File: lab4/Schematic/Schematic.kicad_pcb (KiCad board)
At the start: 2 copper layers, 121.5 x 269.9 mm, 408 parts, among them IC1 TPS564252DRLR, IC2 TPS564252DRLR, IC3 TPS564252DRLR, IC4 TPS564252DRLR, IC5 TPS564252DRLR, IC6 TPS564252DRLR, J1 XT60-M, J10 CANA_Z1, J11 CANA_Z1, J12 CANA_Z1, J13 CANA_Z1, J14 CANA_Z1, J15 CANA_Z1, J16 Conn_01x03_Pin, J17 Conn_01x03_Pin, J18 Barrel_Jack, J2 Z2_SWD, J3 Z2_SWD, J4 Z3_USART, J5 Raspberry_Pi_4, J6 Z3_USART, J7 MOTOR_RIGHT, J8 MOTOR_LEFT, J9 SERVO, Q2 IRF4905, U1 MCP2515-xST, U10 SN65HVD230, U11 MCP2515-xST, U12 SN65HVD230, U13 MCP2515-xST, U14 SN65HVD230, U15 MCP2515-xST, U16 SN65HVD230, U17 MCP2515-xST, U18 SN65HVD230, U2 ACS712xLCTR-05B, U20 L298N, U3 STM32F401RETx, U4 ACS712xLCTR-05B, U5 INA181, U7 STM32F401RETx, U8 SN65HVD230, U9 MCP2515-xST, Y1 CX3225SB16000H0FLJCC, Y2 CX3225SB16000H0FLJCC, Y3 CX3225SB16000H0FLJCC, Y4 CX3225SB16000H0FLJCC, Y5 CX3225SB16000H0FLJCC, Y6 CX3225SB16000H0FLJCC, Y7 ABS25-32.768KHZ-6-T, Y8 ABS25-32.768KHZ-6-T

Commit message: Thicker motor power traces.
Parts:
- moved TP60 20.3 mm to (184.0, -227.5)
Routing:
- net /MOTOR_PWR-_R: track 25.5 -> 18.5 mm
- net /MOTOR_LEFT_PWM: track 66.5 -> 73.1 mm, vias 2 -> 3
- net /Z3_INT_CAN_A: track 53.5 -> 50.0 mm
- net /RL_BLINK: track 76.9 -> 73.8 mm
- net +12V: track 471.8 -> 474.7 mm
- net Net-(D8-DIN): track 94.3 -> 92.0 mm
- net /ENC_LEFT_B: track 121.1 -> 119.5 mm, vias 4 -> 6
- net /STM_POWER_Z3: track 92.1 -> 90.6 mm
- net /Z3_TEST_BUTTON: track 89.3 -> 88.5 mm
- net /Z3_CAN_RX_B: track 14.3 -> 14.9 mm
- net /ENC_LEFT_A: track 79.6 -> 79.8 mm, vias 2 -> 4
- net /MOTOR_PWR+_L: track 43.0 -> 42.8 mm, vias 2 -> 0
- net /MOTOR_CURRENT_LEFT: track 75.2 -> 75.0 mm, vias 2 -> 4
- added copper zone on F.Cu, net /MOTOR_PWR+C_L
- added copper zone on F.Cu, net /MOTOR_PWR+C_R
- added copper zone on F.Cu, net /MOTOR_PWR+_L
- added copper zone on F.Cu, net /MOTOR_PWR+_R
- added copper zone on F.Cu, net /MOTOR_PWR-_L
- added copper zone on F.Cu, net /MOTOR_PWR-_R

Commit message: Power input and protections done with pours.
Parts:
- moved TP86 32.2 mm to (134.5, -144.8)
- moved R86 13.0 mm to (136.8, -163.3), turned to 90 degrees
- moved J17 11.0 mm to (166.7, -138.8)
- moved TP10 8.28 mm to (138.2, -157.0), turned to 180 degrees
- moved D42 7.49 mm to (136.8, -160.3), turned to -90 degrees
- moved R7 7.35 mm to (134.8, -164.0), turned to 90 degrees
- moved TP1 6.18 mm to (183.5, -146.5), turned to 0 degrees
- moved J16 6.14 mm to (191.8, -138.8), turned to -90 degrees
- moved TP2 3.13 mm to (188.0, -146.5), turned to 0 degrees
- moved TP4 2.70 mm to (174.2, -146.5), turned to 0 degrees
- moved TP3 2.50 mm to (178.8, -146.5), turned to 0 degrees
- moved D1 2.02 mm to (134.8, -160.0), turned to 90 degrees
- moved F2 1.70 mm to (150.1, -150.7), turned to 180 degrees
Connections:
- J16 pad 1: +12V -> GND
- J16 pad 3: GND -> +12V
- J17 pad 1: +12V -> GND
- J17 pad 3: GND -> +12V
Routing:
- net Net-(Q2-D): track 47.0 -> 0.00 mm
- net Net-(J1-POS): track 81.2 -> 54.1 mm, vias 1 -> 5
- net +12V: track 474.7 -> 455.1 mm
- net Net-(J16-Pin_2): track 10.6 -> 17.5 mm
- net /UDP_RX: track 22.3 -> 28.7 mm
- net GND: track 365.7 -> 370.3 mm, vias 185 -> 183
- net /Z1_CMD_TX: track 26.3 -> 22.0 mm
- net /Z1_CAN_TX_A: track 5.78 -> 3.45 mm
- net /Z1_CAN_TX_B: track 5.07 -> 2.86 mm
- net Net-(J17-Pin_2): track 13.6 -> 15.2 mm
- net /Z1_INT_CAN_B: track 76.8 -> 75.4 mm
- net /ENC_LEFT_B: track 119.5 -> 120.4 mm
- net /CANL_A: track 205.7 -> 206.5 mm, vias 1 -> 0
- net /CANH_A: track 205.5 -> 206.0 mm
- added copper zone on F.Cu, net +12V
- added copper zone on B.Cu, net Net-(J1-POS)
- added copper zone on F.Cu, net Net-(J1-POS)
- added copper zone on F.Cu, net Net-(Q2-D)

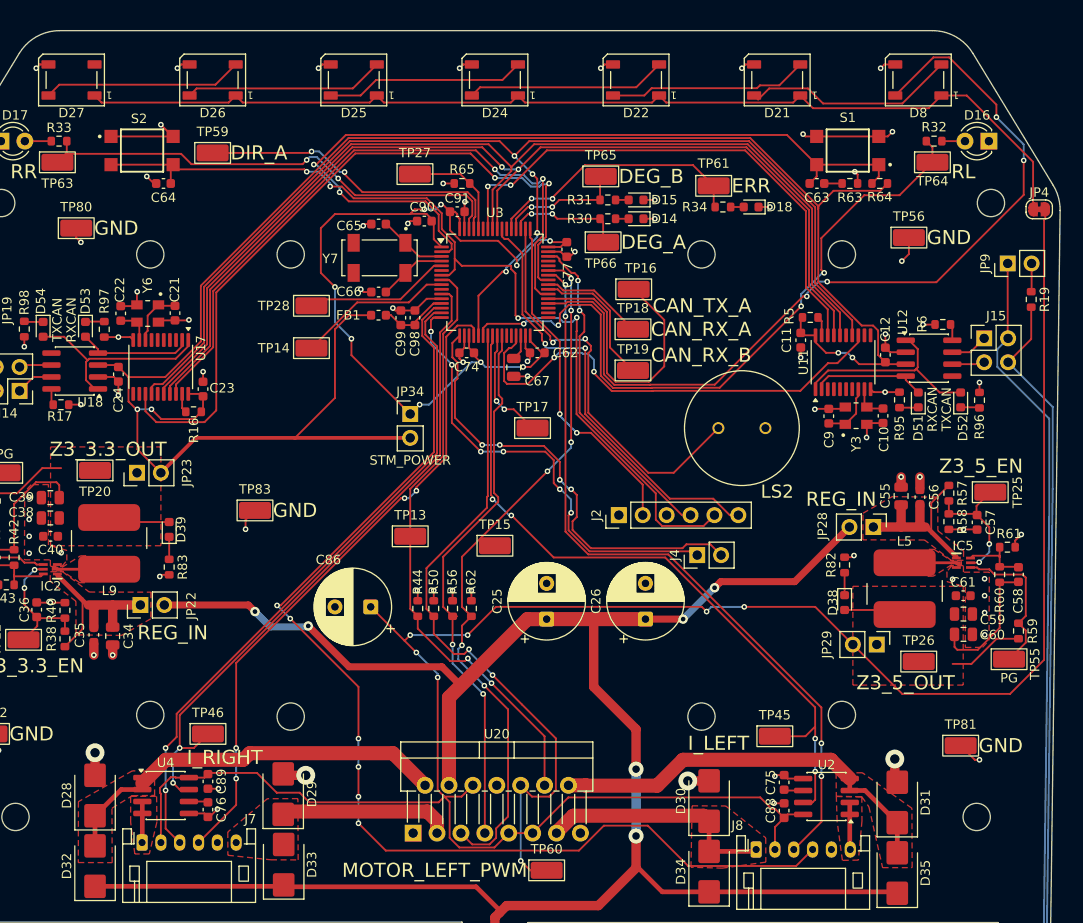
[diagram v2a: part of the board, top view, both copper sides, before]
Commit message: Initial pin assignment change.
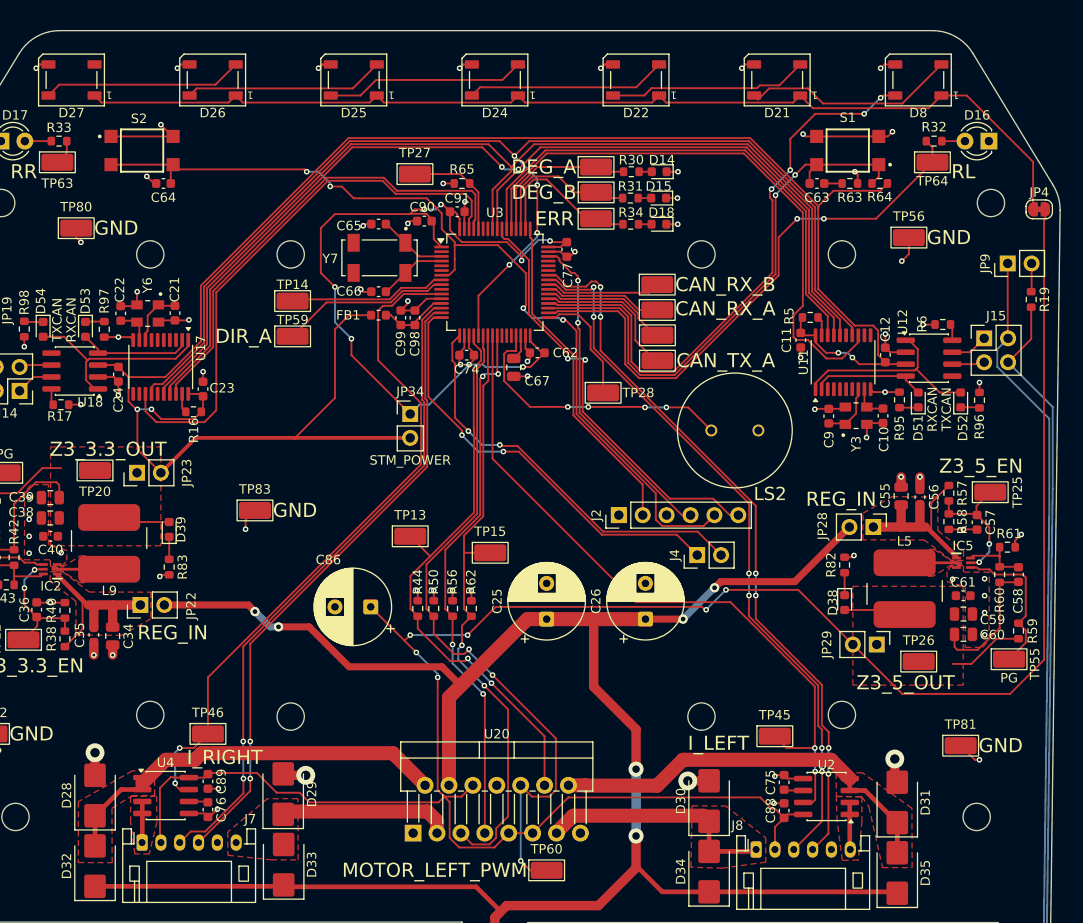
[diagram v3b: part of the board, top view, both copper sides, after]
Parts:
- TP18: value CAN_RX_A -> CAN_RX_B
- TP19: value CAN_RX_B -> CAN_RX_A
- moved TP28 32.4 mm to (190.0, -278.2)
- moved TP59 21.3 mm to (157.0, -284.2)
- moved TP17 16.5 mm to (195.8, -284.4)
- moved TP61 13.0 mm to (189.2, -296.8)
- moved D18 9.97 mm to (195.9, -296.2)
- moved R34 9.97 mm to (192.9, -296.2)
- moved TP66 8.04 mm to (189.2, -302.2)
- moved TP16 7.99 mm to (195.8, -281.7)
- moved TP19 6.93 mm to (195.8, -287.1)
- moved R30 5.59 mm to (193.0, -301.8)
- moved D14 5.57 mm to (196.0, -301.8)
- moved TP18 5.40 mm to (195.8, -289.8)
- moved TP14 5.39 mm to (157.0, -288.0)
- moved D15 2.41 mm to (195.9, -298.9)
- moved R31 2.41 mm to (192.9, -298.9)
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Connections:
- LS2 pad 1: unconnected-(LS2-Pad1) -> Net-(U3-PB10)
- TP14 pad 1: /PWM_SET -> Net-(U3-PC0)
- TP18 pad 1: /Z3_CAN_RX_A -> /Z3_CAN_RX_B
- TP19 pad 1: /Z3_CAN_RX_B -> /Z3_CAN_RX_A
- TP28 pad 1: Net-(U3-PH0) -> Net-(U3-PB12)
- TP59 pad 1: /DIR_A -> Net-(U3-PC1)
- U3 pad 14: /ENC_LEFT_B -> /ENC_RIGHT_A
- U3 pad 15: /ENC_RIGHT_A -> /ENC_RIGHT_B
- U3 pad 2: /Z3_TEST_BUTTON -> /RR_BLINKER
- U3 pad 20: /ENC_RIGHT_B -> /MOTOR_LEFT_DIR
- U3 pad 22: /RL_BLINK -> /MOTOR_LEFT_PWM
- U3 pad 23: /MOTOR_LEFT_PWM -> /MOTOR_RIGHT_PWM
- U3 pad 25: /Z3_CAN_TX_B -> /MOTOR_RIGHT_DIR
- U3 pad 26: /MOTOR_RIGHT_DIR -> unconnected-(U3-PB0-Pad26)
- U3 pad 29: /Z3_INT_CAN_A -> Net-(U3-PB10)
- U3 pad 33: unconnected-(U3-PB12-Pad33) -> Net-(U3-PB12)
- U3 pad 34: unconnected-(U3-PB13-Pad34) -> /RL_BLINK
- U3 pad 35: unconnected-(U3-PB14-Pad35) -> /Z3_TEST_BUTTON
- U3 pad 38: /Z3_CS_CAN_B -> /Z3_CAN_TX_B
- U3 pad 39: /Z3_CAN_RX_B -> /Z3_CAN_RX_A
- U3 pad 40: /Z3_CAN_RX_A -> /Z3_CAN_RX_B
- U3 pad 41: /Z3_INT_CAN_B -> /ENC_LEFT_A
- U3 pad 42: /ENC_LEFT_A -> /ENC_LEFT_B
- U3 pad 43: /MOTOR_RIGHT_PWM -> unconnected-(U3-PA10-Pad43)
- U3 pad 5: Net-(U3-PH0) -> unconnected-(U3-PH0-Pad5)
- U3 pad 50: unconnected-(LS2-Pad1) -> /Z3_ERR
- U3 pad 51: /Z3_DEG_A -> /Z3_DEG_B
- U3 pad 52: /Z3_DEG_B -> /Z3_DEG_A
- U3 pad 53: /Z3_ERR -> /Z3_INT_CAN_A
- U3 pad 54: unconnected-(U3-PD2-Pad54) -> /Z3_CS_CAN_A
- U3 pad 58: /Z3_CS_CAN_A -> unconnected-(U3-PB6-Pad58)
- U3 pad 61: /DIR_A -> /Z3_CS_CAN_B
- U3 pad 62: /RR_BLINK -> /Z3_INT_CAN_B
- U3 pad 8: /MOTOR_LEFT_DIR -> Net-(U3-PC0)
- U3 pad 9: /PWM_SET -> Net-(U3-PC1)
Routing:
- net /RR_BLINK: track 52.9 -> 2.66 mm, vias 2 -> 0
- net unconnected-(LS2-Pad1): track 43.5 -> 0.00 mm, vias 2 -> 0
- net /ENC_LEFT_B: track 120.4 -> 77.1 mm
- net /DIR_A: track 33.4 -> 0.00 mm, vias 2 -> 0
- net Net-(U3-PB10): track 0.00 -> 30.1 mm, vias 0 -> 4
- net Net-(D8-DIN): track 92.0 -> 62.4 mm
- net /Z3_TEST_BUTTON: track 88.5 -> 59.8 mm
- net /Z3_CS_CAN_B: track 69.1 -> 49.9 mm, vias 2 -> 0
- net /Z3_INT_CAN_B: track 77.6 -> 59.0 mm, vias 2 -> 0
- net Net-(U3-PC1): track 0.00 -> 18.1 mm
- net Net-(U3-PC0): track 0.00 -> 16.8 mm
- net /PWM_SET: track 16.6 -> 0.00 mm
- net Net-(U3-PH0): track 15.6 -> 0.00 mm
- net /Z3_CAN_TX_A: track 30.0 -> 15.9 mm
- net /RL_BLINK: track 73.8 -> 61.1 mm, vias 4 -> 2
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
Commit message: Fixed ENC and CAN_INT exti cofnflict.
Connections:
- U3 pad 58: unconnected-(U3-PB6-Pad58) -> /Z3_CS_CAN_B
- U3 pad 59: unconnected-(U3-PB7-Pad59) -> /Z3_INT_CAN_B
- U3 pad 61: /Z3_CS_CAN_B -> unconnected-(U3-PB8-Pad61)
- U3 pad 62: /Z3_INT_CAN_B -> unconnected-(U3-PB9-Pad62)
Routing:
- net /Z3_INT_CAN_B: track 59.0 -> 65.0 mm
- net /Z3_CS_CAN_B: track 49.9 -> 55.6 mm
